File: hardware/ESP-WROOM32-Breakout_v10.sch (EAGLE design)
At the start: 45 parts, among them IC1 CP2102N-QFN24, IC2 VREG-TS1117CW-3V3, J1 MA19-1, J2 MA19-1, T1 BSS138PS, X1 PASSER-07, X2 PASSER-07, X3 PASSER-07, X4 PASSER-07

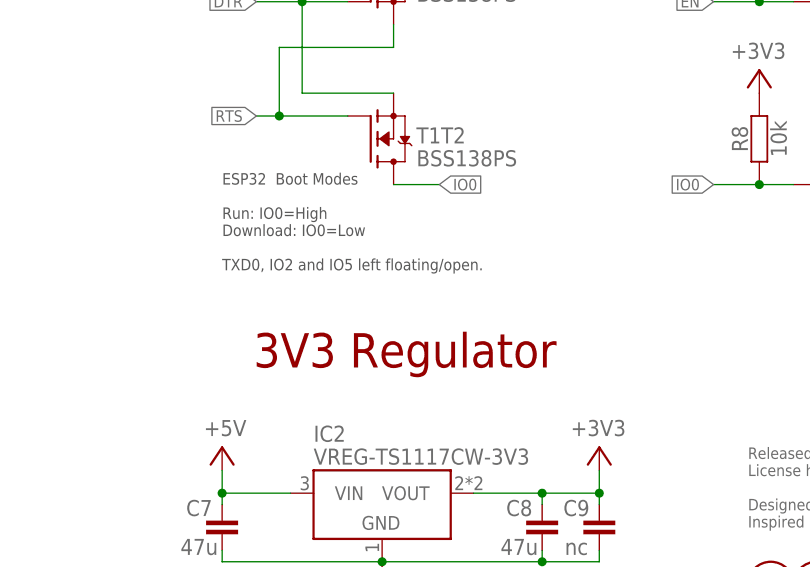
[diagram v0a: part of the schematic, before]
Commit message: updated schematics
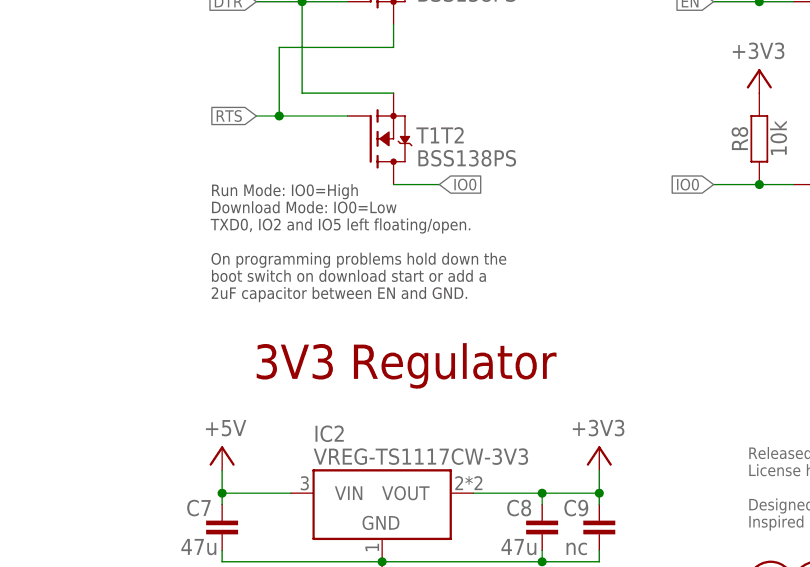
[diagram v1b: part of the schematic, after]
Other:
- note added: "Run Mode: IO0=High Download Mode: IO0=Low TXD0, IO2 and IO5 left floating/open. On programming problems hold down the boot switch on download start or add a 2uF capacitor between EN and GND."
- note removed: "ESP32 Boot Modes Run: IO0=High Download: IO0=Low TXD0, IO2 and IO5 left floating/open."
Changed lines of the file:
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@@
 <setting verticaltext="up"/>
 </settings>
-<grid distance="0.1" unitdist="inch" unit="inch" style="lines" multiple="1" display="no" altdistance="0.01" altunitdist="inch" altunit="inch"/>
+<grid distance="0.05" unitdist="inch" unit="inch" style="lines" multiple="1" display="yes" altdistance="0.025" altunitdist="inch" altunit="inch"/>
 <layers>
 <layer number="1" name="Top" color="4" fill="1" visible="no" active="no"/>
@@
 <text x="121.92" y="90.17" size="3.81" layer="94" align="bottom-center">Programming Logic</text>
 <text x="49.53" y="161.29" size="3.81" layer="94" align="bottom-center">ESP-WROOM-32</text>
-<text x="124.46" y="31.75" size="3.81" layer="94" align="bottom-center">3V3 Regulator</text>
-<text x="104.14" y="53.34" size="1.27" layer="97" align="top-left">ESP32  Boot Modes
-Run: IO0=High
-Download: IO0=Low
-TXD0, IO2 and IO5 left floating/open.</text>
+<text x="124.46" y="30.48" size="3.81" layer="94" align="bottom-center">3V3 Regulator</text>
+<text x="102.87" y="52.07" size="1.27" layer="97" align="top-left">Run Mode: IO0=High
+Download Mode: IO0=Low
+TXD0, IO2 and IO5 left floating/open.
+On programming problems hold down the
+boot switch on download start or add a
+2uF capacitor between EN and GND.</text>
 </plain>
 <instances>
